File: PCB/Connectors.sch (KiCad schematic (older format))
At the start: 5 parts

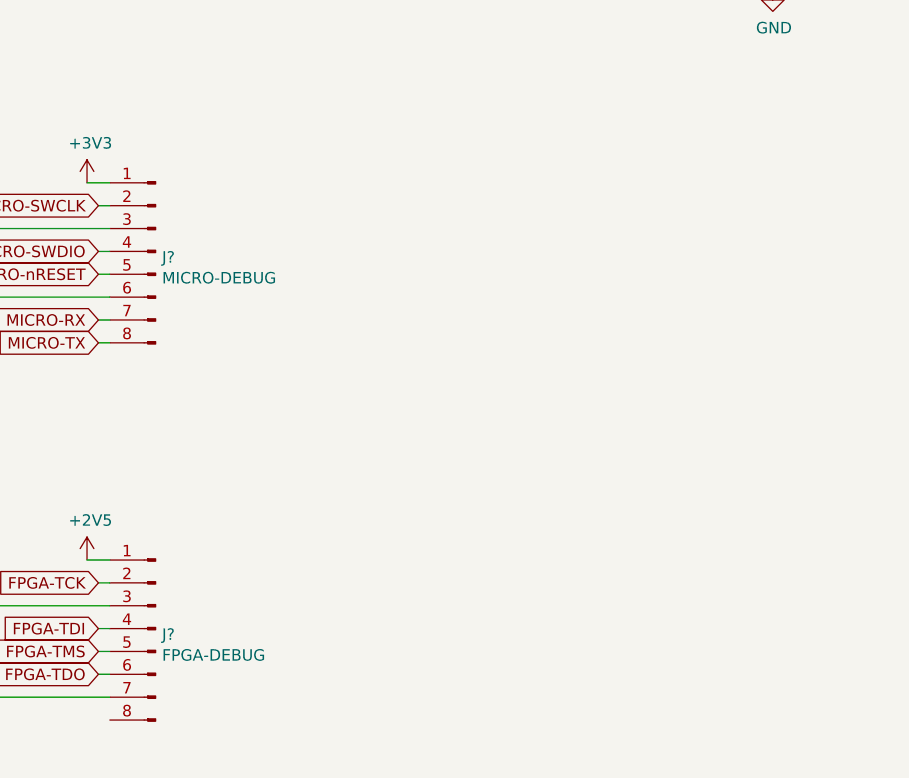
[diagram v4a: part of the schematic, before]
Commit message: Connect LED to microcontroller, add another debugging header
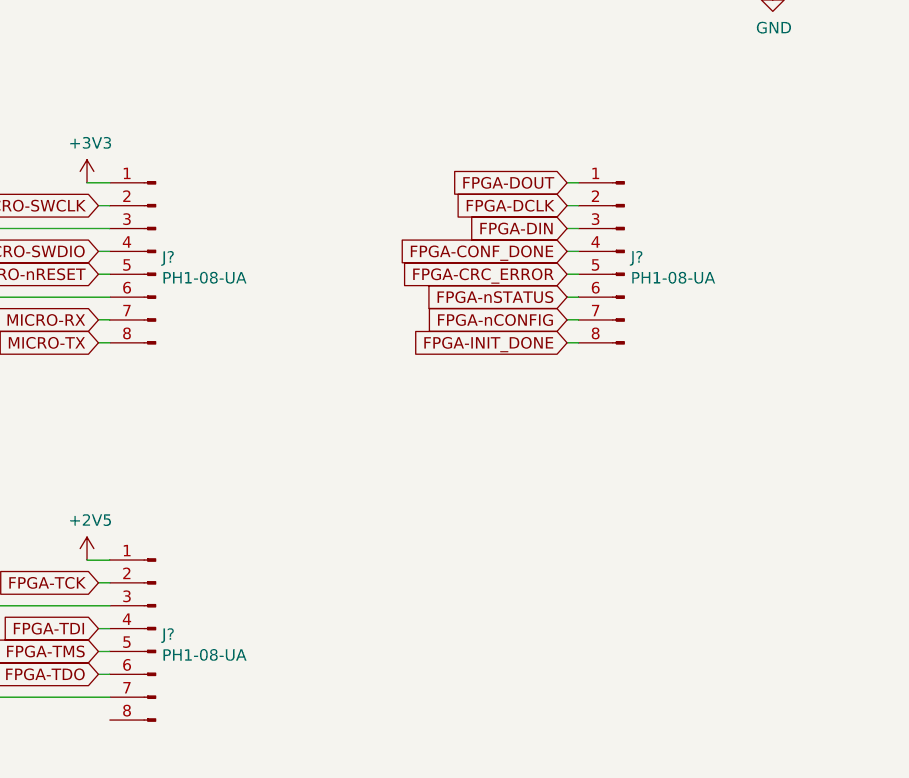
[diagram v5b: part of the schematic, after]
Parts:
- added J?: PH1-08-UA, Pin_Headers:Pin_Header_Straight_1x08_Pitch2.54mm, symbol Connector:Conn_01x08_Male
- J?: value MICRO-DEBUG -> PH1-08-UA
- J?: value FPGA-DEBUG -> PH1-08-UA
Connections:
- new net FPGA-CONF_DONE: J?.4 (Pin_4)
- new net FPGA-CRC_ERROR: J?.5 (Pin_5)
- new net FPGA-DCLK: J?.2 (Pin_2)
- new net FPGA-DIN: J?.3 (Pin_3)
- new net FPGA-DOUT: J?.1 (Pin_1)
- new net FPGA-INIT_DONE: J?.8 (Pin_8)
- new net FPGA-nCONFIG: J?.7 (Pin_7)
- new net FPGA-nSTATUS: J?.6 (Pin_6)
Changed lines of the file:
@@
 P 3000 4200
 F 0 "J?" H 2972 4174 50  0000 R CNN
-F 1 "MICRO-DEBUG" H 2972 4083 50  0000 R CNN
+F 1 "PH1-08-UA" H 2972 4083 50  0000 R CNN
 F 2 "Pin_Headers:Pin_Header_Straight_1x08_Pitch2.54mm" H 3000 4200 50  0001 C CNN
 F 3 "https://www.digikey.ca/product-detail/en/adam-tech/PH1-08-UA/2057-PH1-08-UA-ND/9830442" H 3000 4200 50  0001 C CNN
@@
 P 3000 5850
 F 0 "J?" H 2972 5824 50  0000 R CNN
-F 1 "FPGA-DEBUG" H 2972 5733 50  0000 R CNN
+F 1 "PH1-08-UA" H 2972 5733 50  0000 R CNN
 F 2 "Pin_Headers:Pin_Header_Straight_1x08_Pitch2.54mm" H 3000 5850 50  0001 C CNN
 F 3 "https://www.digikey.ca/product-detail/en/adam-tech/PH1-08-UA/2057-PH1-08-UA-ND/9830442" H 3000 5850 50  0001 C CNN
@@
 	1    0    0    -1
 $EndComp
+$Comp
+L Connector:Conn_01x08_Male J?
+U 1 1 5DF84ABE
+P 5050 4200
+F 0 "J?" H 5022 4174 50  0000 R CNN
+F 1 "PH1-08-UA" H 5022 4083 50  0000 R CNN
+F 2 "Pin_Headers:Pin_Header_Straight_1x08_Pitch2.54mm" H 5050 4200 50  0001 C CNN
+F 3 "https://www.digikey.ca/product-detail/en/adam-tech/PH1-08-UA/2057-PH1-08-UA-ND/9830442" H 5050 4200 50  0001 C CNN
+	1    5050 4200
+	-1   0    0    -1
+$EndComp
+Text GLabel 4800 3900 0    50   Input ~ 0
+FPGA-DOUT
+Text GLabel 4800 4400 0    50   Input ~ 0
+FPGA-nSTATUS
+Text GLabel 4800 4000 0    50   Input ~ 0
+FPGA-DCLK
+Text GLabel 4800 4100 0    50   Input ~ 0
+FPGA-DIN
+Text GLabel 4800 4500 0    50   Input ~ 0
+FPGA-nCONFIG
+Text GLabel 4800 4200 0    50   Input ~ 0
+FPGA-CONF_DONE
+Text GLabel 4800 4600 0    50   Input ~ 0
+FPGA-INIT_DONE
+Text GLabel 4800 4300 0    50   Input ~ 0
+FPGA-CRC_ERROR
+Wire Wire Line
+	4800 3900 4850 3900
+Wire Wire Line
+	4850 4000 4800 4000
+Wire Wire Line
+	4800 4100 4850 4100
+Wire Wire Line
+	4850 4200 4800 4200
+Wire Wire Line
+	4800 4300 4850 4300
+Wire Wire Line
+	4850 4400 4800 4400
+Wire Wire Line
+	4800 4500 4850 4500
+Wire Wire Line
+	4850 4600 4800 4600
 $EndSCHEMATC

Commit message: Add connectors for all power supplies
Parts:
- added J? (x4): DNP, Pin_Headers:Pin_Header_Straight_1x02_Pitch2.54mm, symbol Connector:Conn_01x02_Male
- added J?: DNP, Pin_Headers:Pin_Header_Straight_1x08_Pitch2.54mm, symbol Connector:Conn_01x08_Male
- J?: value PH1-08-UA -> DNP
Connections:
- net GND: now also J?.1 (Pin_1), J?.1 (Pin_1), J?.1 (Pin_1), J?.1 (Pin_1)
- new net +12V: J?.2 (Pin_2)
- new net +1V2: J?.2 (Pin_2)
- new net +50V: J?.2 (Pin_2)
- new net +9V: J?.2 (Pin_2)
- new net FPGA-LINK0: J?.1 (Pin_1)
- new net FPGA-LINK1: J?.2 (Pin_2)
- new net FPGA-LINK2: J?.3 (Pin_3)
- new net FPGA-LINK3: J?.4 (Pin_4)
- new net FPGA-LINK4: J?.5 (Pin_5)
- new net FPGA-LINK5: J?.6 (Pin_6)
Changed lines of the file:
@@
 P 5050 4200
 F 0 "J?" H 5022 4174 50  0000 R CNN
-F 1 "PH1-08-UA" H 5022 4083 50  0000 R CNN
+F 1 "DNP" H 5022 4083 50  0000 R CNN
 F 2 "Pin_Headers:Pin_Header_Straight_1x08_Pitch2.54mm" H 5050 4200 50  0001 C CNN
 F 3 "https://www.digikey.ca/product-detail/en/adam-tech/PH1-08-UA/2057-PH1-08-UA-ND/9830442" H 5050 4200 50  0001 C CNN
@@
 Wire Wire Line
 	4850 4600 4800 4600
+$Comp
+L Connector:Conn_01x02_Male J?
+U 1 1 5DEC9B64
+P 6500 4000
+F 0 "J?" H 6472 3882 50  0000 R CNN
+F 1 "DNP" H 6472 3973 50  0000 R CNN
+F 2 "Pin_Headers:Pin_Header_Straight_1x02_Pitch2.54mm" H 6500 4000 50  0001 C CNN
+F 3 "https://www.digikey.ca/product-detail/en/adam-tech/PH1-02-UA/2057-PH1-02-UA-ND/9830266" H 6500 4000 50  0001 C CNN
+	1    6500 4000
+	-1   0    0    1
+$EndComp
+$Comp
+L power:+1V2 #PWR?
+U 1 1 5DECE3B1
+P 6200 3900
+F 0 "#PWR?" H 6200 3750 50  0001 C CNN
+F 1 "+1V2" H 6215 4073 50  0000 C CNN
+F 2 "" H 6200 3900 50  0001 C CNN
+F 3 "" H 6200 3900 50  0001 C CNN
+	1    6200 3900
+	1    0    0    -1
+$EndComp
+Wire Wire Line
+	6200 3900 6300 3900
+$Comp
+L power:GND #PWR?
+U 1 1 5DECF8CC
+P 6200 4000
+F 0 "#PWR?" H 6200 3750 50  0001 C CNN
+F 1 "GND" H 6205 3827 50  0000 C CNN
+F 2 "" H 6200 4000 50  0001 C CNN
+F 3 "" H 6200 4000 50  0001 C CNN
+	1    6200 4000
+	1    0    0    -1
+$EndComp
+Wire Wire Line
+	6200 4000 6300 4000
+$Comp
+L Connector:Conn_01x02_Male J?
+U 1 1 5DED29C8
+P 6500 5300
+F 0 "J?" H 6472 5182 50  0000 R CNN
+F 1 "DNP" H 6472 5273 50  0000 R CNN
+F 2 "Pin_Headers:Pin_Header_Straight_1x02_Pitch2.54mm" H 6500 5300 50  0001 C CNN
+F 3 "https://www.digikey.ca/product-detail/en/adam-tech/PH1-02-UA/2057-PH1-02-UA-ND/9830266" H 6500 5300 50  0001 C CNN
+	1    6500 5300
+	-1   0    0    1
+$EndComp
+Wire Wire Line
+	6200 5200 6300 5200
+$Comp
+L power:GND #PWR?
+U 1 1 5DED29DD
+P 6200 5300
+F 0 "#PWR?" H 6200 5050 50  0001 C CNN
+F 1 "GND" H 6205 5127 50  0000 C CNN
+F 2 "" H 6200 5300 50  0001 C CNN
+F 3 "" H 6200 5300 50  0001 C CNN
+	1    6200 5300
+	1    0    0    -1
+$EndComp
+Wire Wire Line
+	6200 5300 6300 5300
+$Comp
+L power:+12V #PWR?
+U 1 1 5DED51C9
+P 6200 5200
+F 0 "#PWR?" H 6200 5050 50  0001 C CNN
+F 1 "+12V" H 6215 5373 50  0000 C CNN
+F 2 "" H 6200 5200 50  0001 C CNN
+F 3 "" H 6200 5200 50  0001 C CNN
+	1    6200 5200
+	1    0    0    -1
+$EndComp
+$Comp
+L Connector:Conn_01x02_Male J?
+U 1 1 5DED5F02
+P 6500 5950
+F 0 "J?" H 6472 5832 50  0000 R CNN
+F 1 "DNP" H 6472 5923 50  0000 R CNN
+F 2 "Pin_Headers:Pin_Header_Straight_1x02_Pitch2.54mm" H 6500 5950 50  0001 C CNN
+F 3 "https://www.digikey.ca/product-detail/en/adam-tech/PH1-02-UA/2057-PH1-02-UA-ND/9830266" H 6500 5950 50  0001 C CNN
+	1    6500 5950
+	-1   0    0    1
+$EndComp
+Wire Wire Line
+	6200 5850 6300 5850
+$Comp
+L power:GND #PWR?
+U 1 1 5DED5F0D
+P 6200 5950
+F 0 "#PWR?" H 6200 5700 50  0001 C CNN
+F 1 "GND" H 6205 5777 50  0000 C CNN
+F 2 "" H 6200 5950 50  0001 C CNN
+F 3 "" H 6200 5950 50  0001 C CNN
+	1    6200 5950
+	1    0    0    -1
+$EndComp
+Wire Wire Line
+	6200 5950 6300 5950
+$Comp
+L Parts:+50V #PWR?
+U 1 1 5DED7ED3
+P 6200 5850
+F 0 "#PWR?" H 6200 5700 50  0001 C CNN
+F 1 "+50V" H 6215 6023 50  0000 C CNN
+F 2 "" H 6200 5850 50  0001 C CNN
+F 3 "" H 6200 5850 50  0001 C CNN
+	1    6200 5850
+	1    0    0    -1
+$EndComp
+$Comp
+L Connector:Conn_01x08_Male J?
+U 1 1 5DEE094B
+P 5050 5850
+F 0 "J?" H 5022 5824 50  0000 R CNN
+F 1 "DNP" H 5022 5733 50  0000 R CNN
+F 2 "Pin_Headers:Pin_Header_Straight_1x08_Pitch2.54mm" H 5050 5850 50  0001 C CNN
+F 3 "https://www.digikey.ca/product-detail/en/adam-tech/PH1-08-UA/2057-PH1-08-UA-ND/9830442" H 5050 5850 50  0001 C CNN
+	1    5050 5850
+	-1   0    0    -1
+$EndComp
+Text GLabel 4800 5550 0    50   Input ~ 0
+FPGA-LINK0
+Text GLabel 4800 5650 0    50   Input ~ 0
+FPGA-LINK1
+Text GLabel 4800 5750 0    50   Input ~ 0
+FPGA-LINK2
+Text GLabel 4800 5850 0    50   Input ~ 0
+FPGA-LINK3
+Text GLabel 4800 5950 0    50   Input ~ 0
+FPGA-LINK4
+Text GLabel 4800 6050 0    50   Input ~ 0
+FPGA-LINK5
+Wire Wire Line
+	4800 5550 4850 5550
+Wire Wire Line
+	4850 5650 4800 5650
+Wire Wire Line
+	4800 5750 4850 5750
+Wire Wire Line
+	4800 5850 4850 5850
+Wire Wire Line
+	4850 5950 4800 5950
+Wire Wire Line
+	4800 6050 4850 6050
+$Comp
+L Connector:Conn_01x02_Male J?
+U 1 1 5DEFA66E
+P 6500 4650
+F 0 "J?" H 6472 4532 50  0000 R CNN
+F 1 "DNP" H 6472 4623 50  0000 R CNN
+F 2 "Pin_Headers:Pin_Header_Straight_1x02_Pitch2.54mm" H 6500 4650 50  0001 C CNN
+F 3 "https://www.digikey.ca/product-detail/en/adam-tech/PH1-02-UA/2057-PH1-02-UA-ND/9830266" H 6500 4650 50  0001 C CNN
+	1    6500 4650
+	-1   0    0    1
+$EndComp
+$Comp
+L power:GND #PWR?
+U 1 1 5DEFAC45
+P 6200 4650
+F 0 "#PWR?" H 6200 4400 50  0001 C CNN
+F 1 "GND" H 6205 4477 50  0000 C CNN
+F 2 "" H 6200 4650 50  0001 C CNN
+F 3 "" H 6200 4650 50  0001 C CNN
+	1    6200 4650
+	1    0    0    -1
+$EndComp
+Wire Wire Line
+	6200 4650 6300 4650
+Wire Wire Line
+	6300 4550 6200 4550
+$Comp
+L power:+9V #PWR?
+U 1 1 5DEFE9A9
+P 6200 4550
+F 0 "#PWR?" H 6200 4400 50  0001 C CNN
+F 1 "+9V" H 6215 4723 50  0000 C CNN
+F 2 "" H 6200 4550 50  0001 C CNN
+F 3 "" H 6200 4550 50  0001 C CNN
+	1    6200 4550
+	1    0    0    -1
+$EndComp
 $EndSCHEMATC

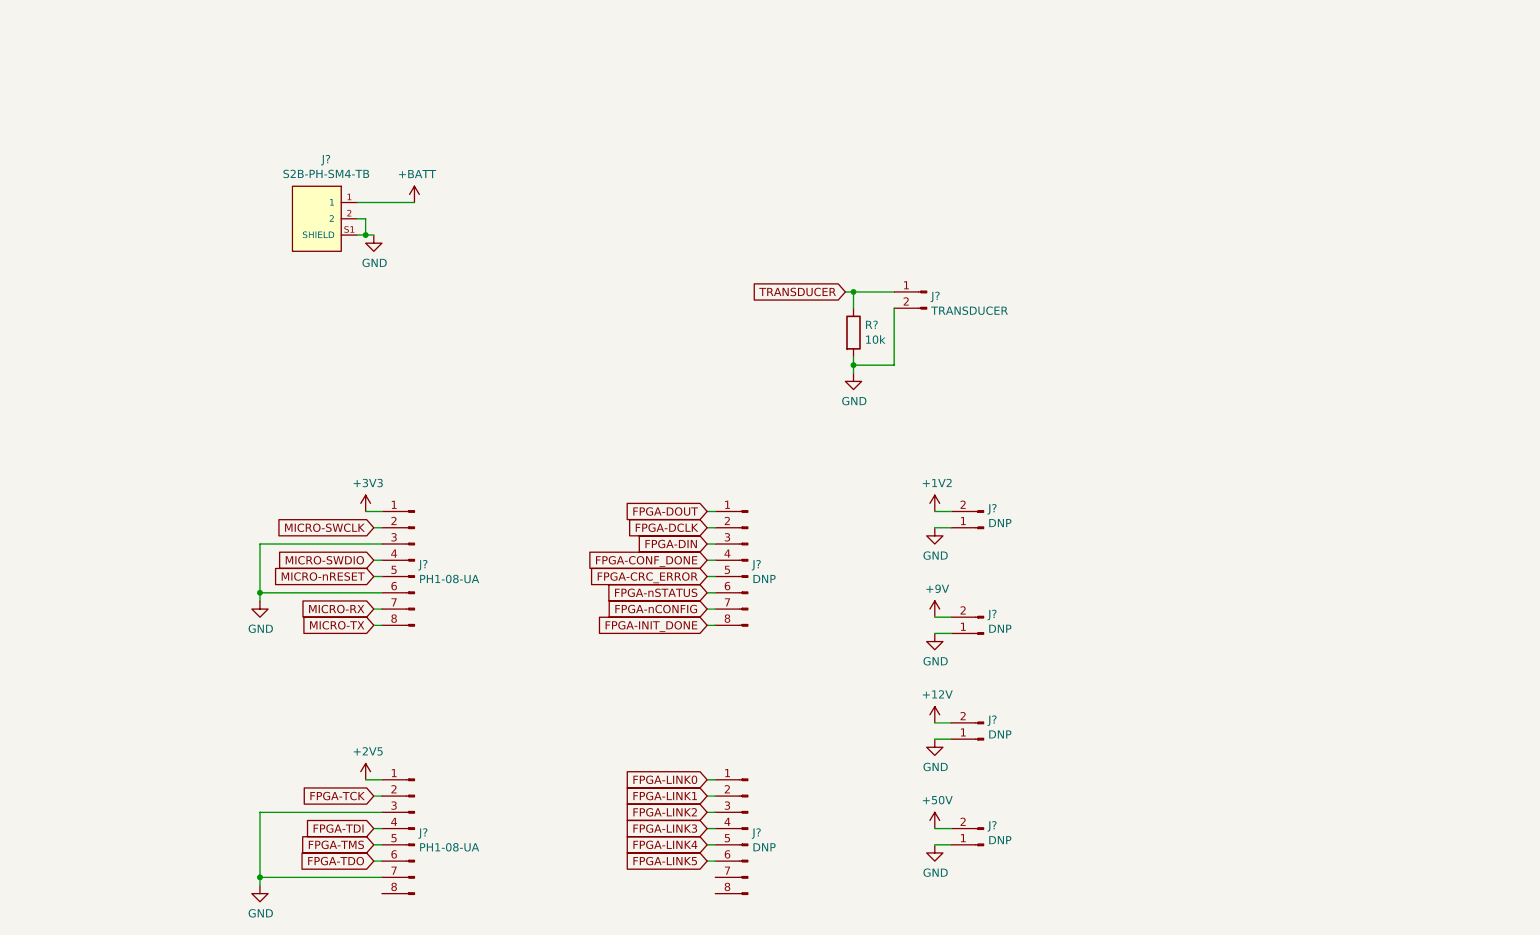
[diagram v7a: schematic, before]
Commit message: Bring additional signals to the connectors sheet for debug access
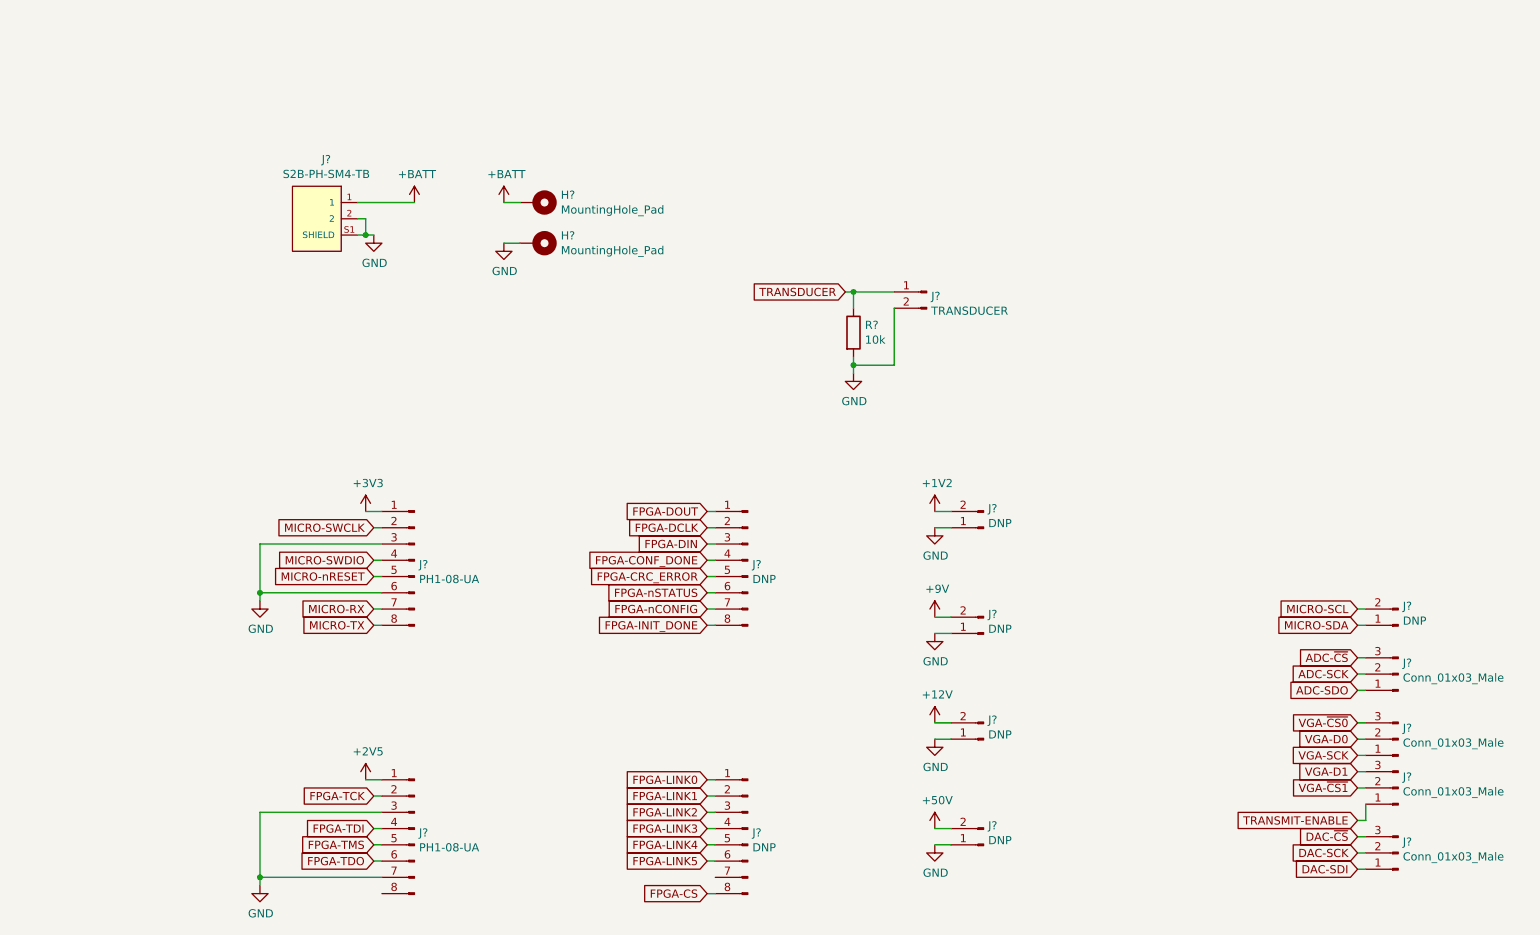
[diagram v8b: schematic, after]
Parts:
- added H? (x2): MountingHole_Pad, symbol Mechanical:MountingHole_Pad
- added J?: DNP, Pin_Headers:Pin_Header_Straight_1x02_Pitch2.54mm, symbol Connector:Conn_01x02_Male
- added J? (x4): Conn_01x03_Male, symbol Connector:Conn_01x03_Male
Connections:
- net +BATT: now also H?.1
- net GND: now also H?.1
- net FPGA-CS: now reaches J?.8 (Pin_8)
- new net ADC-SCK: J?.2 (Pin_2)
- new net ADC-SDO: J?.1 (Pin_1)
- new net ADC-~CS: J?.3 (Pin_3)
- new net DAC-SCK: J?.2 (Pin_2)
- new net DAC-SDI: J?.1 (Pin_1)
- new net DAC-~CS: J?.3 (Pin_3)
- new net MICRO-SCL: J?.2 (Pin_2)
- new net MICRO-SDA: J?.1 (Pin_1)
- new net TRANSMIT-ENABLE: J?.1 (Pin_1)
- new net VGA-D0: J?.2 (Pin_2)
- new net VGA-D1: J?.3 (Pin_3)
- new net VGA-SCK: J?.1 (Pin_1)
- new net VGA-~CS0: J?.3 (Pin_3)
- new net VGA-~CS1: J?.2 (Pin_2)
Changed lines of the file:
@@
 	1    0    0    -1
 $EndComp
+Text GLabel 4800 6250 0    50   Input ~ 0
+FPGA-CS
+Text GLabel 8800 4500 0    50   Input ~ 0
+MICRO-SCL
+Text GLabel 8800 4600 0    50   Input ~ 0
+MICRO-SDA
+Text GLabel 8800 4800 0    50   Input ~ 0
+ADC-~CS
+Text GLabel 8800 4900 0    50   Input ~ 0
+ADC-SCK
+Text GLabel 8800 5000 0    50   Input ~ 0
+ADC-SDO
+Text GLabel 8800 5200 0    50   Input ~ 0
+VGA-~CS0
+Text GLabel 8800 5300 0    50   Input ~ 0
+VGA-D0
+Text GLabel 8800 5400 0    50   Input ~ 0
+VGA-SCK
+Text GLabel 8800 5500 0    50   Input ~ 0
+VGA-D1
+Text GLabel 8800 5600 0    50   Input ~ 0
+VGA-~CS1
+Text GLabel 8800 5900 0    50   Input ~ 0
+DAC-~CS
+Text GLabel 8800 6000 0    50   Input ~ 0
+DAC-SCK
+Text GLabel 8800 6100 0    50   Input ~ 0
+DAC-SDI
+Text GLabel 8800 5800 0    50   Input ~ 0
+TRANSMIT-ENABLE
+Wire Wire Line
+	4800 6250 4850 6250
+$Comp
+L Connector:Conn_01x02_Male J?
+U 1 1 5E2272DF
+P 9050 4600
+F 0 "J?" H 9022 4482 50  0000 R CNN
+F 1 "DNP" H 9022 4573 50  0000 R CNN
+F 2 "Pin_Headers:Pin_Header_Straight_1x02_Pitch2.54mm" H 9050 4600 50  0001 C CNN
+F 3 "https://www.digikey.ca/product-detail/en/adam-tech/PH1-02-UA/2057-PH1-02-UA-ND/9830266" H 9050 4600 50  0001 C CNN
+	1    9050 4600
+	-1   0    0    1
+$EndComp
+Wire Wire Line
+	8850 4500 8800 4500
+Wire Wire Line
+	8800 4600 8850 4600
+$Comp
+L Connector:Conn_01x03_Male J?
+U 1 1 5E22DC4D
+P 9050 4900
+F 0 "J?" H 9022 4832 50  0000 R CNN
+F 1 "Conn_01x03_Male" H 9022 4923 50  0000 R CNN
+F 2 "" H 9050 4900 50  0001 C CNN
+F 3 "~" H 9050 4900 50  0001 C CNN
+	1    9050 4900
+	-1   0    0    1
+$EndComp
+Wire Wire Line
+	8800 4800 8850 4800
+Wire Wire Line
+	8850 4900 8800 4900
+Wire Wire Line
+	8800 5000 8850 5000
+$Comp
+L Connector:Conn_01x03_Male J?
+U 1 1 5E232910
+P 9050 5300
+F 0 "J?" H 9022 5232 50  0000 R CNN
+F 1 "Conn_01x03_Male" H 9022 5323 50  0000 R CNN
+F 2 "" H 9050 5300 50  0001 C CNN
+F 3 "~" H 9050 5300 50  0001 C CNN
+	1    9050 5300
+	-1   0    0    1
+$EndComp
+Wire Wire Line
+	8800 5200 8850 5200
+Wire Wire Line
+	8800 5300 8850 5300
+Wire Wire Line
+	8800 5400 8850 5400
+$Comp
+L Connector:Conn_01x03_Male J?
+U 1 1 5E236FC5
+P 9050 5600
+F 0 "J?" H 9022 5532 50  0000 R CNN
+F 1 "Conn_01x03_Male" H 9022 5623 50  0000 R CNN
+F 2 "" H 9050 5600 50  0001 C CNN
+F 3 "~" H 9050 5600 50  0001 C CNN
+	1    9050 5600
+	-1   0    0    1
+$EndComp
+Wire Wire Line
+	8800 5500 8850 5500
+Wire Wire Line
+	8850 5600 8800 5600
+Wire Wire Line
+	8800 5800 8850 5800
+Wire Wire Line
+	8850 5800 8850 5700
+$Comp
+L Connector:Conn_01x03_Male J?
+U 1 1 5E23BCC1
+P 9050 6000
+F 0 "J?" H 9022 5932 50  0000 R CNN
+F 1 "Conn_01x03_Male" H 9022 6023 50  0000 R CNN
+F 2 "" H 9050 6000 50  0001 C CNN
+F 3 "~" H 9050 6000 50  0001 C CNN
+	1    9050 6000
+	-1   0    0    1
+$EndComp
+Wire Wire Line
+	8800 5900 8850 5900
+Wire Wire Line
+	8800 6000 8850 6000
+Wire Wire Line
+	8800 6100 8850 6100
+$Comp
+L Mechanical:MountingHole_Pad H?
+U 1 1 5E24249E
+P 3750 2250
+F 0 "H?" V 3704 2400 50  0000 L CNN
+F 1 "MountingHole_Pad" V 3795 2400 50  0000 L CNN
+F 2 "" H 3750 2250 50  0001 C CNN
+F 3 "~" H 3750 2250 50  0001 C CNN
+	1    3750 2250
+	0    1    1    0
+$EndComp
+$Comp
+L power:GND #PWR?
+U 1 1 5E243B36
+P 3550 2250
+F 0 "#PWR?" H 3550 2000 50  0001 C CNN
+F 1 "GND" H 3555 2077 50  0000 C CNN
+F 2 "" H 3550 2250 50  0001 C CNN
+F 3 "" H 3550 2250 50  0001 C CNN
+	1    3550 2250
+	1    0    0    -1
+$EndComp
+Wire Wire Line
+	3550 2250 3650 2250
+$Comp
+L Mechanical:MountingHole_Pad H?
+U 1 1 5E246FF3
+P 3750 2000
+F 0 "H?" V 3704 2150 50  0000 L CNN
+F 1 "MountingHole_Pad" V 3795 2150 50  0000 L CNN
+F 2 "" H 3750 2000 50  0001 C CNN
+F 3 "~" H 3750 2000 50  0001 C CNN
+	1    3750 2000
+	0    1    1    0
+$EndComp
+$Comp
+L power:+BATT #PWR?
+U 1 1 5E24725E
+P 3550 2000
+F 0 "#PWR?" H 3550 1850 50  0001 C CNN
+F 1 "+BATT" H 3565 2173 50  0000 C CNN
+F 2 "" H 3550 2000 50  0001 C CNN
+F 3 "" H 3550 2000 50  0001 C CNN
+	1    3550 2000
+	1    0    0    -1
+$EndComp
+Wire Wire Line
+	3550 2000 3650 2000
 $EndSCHEMATC
